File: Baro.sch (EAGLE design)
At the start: 9 parts

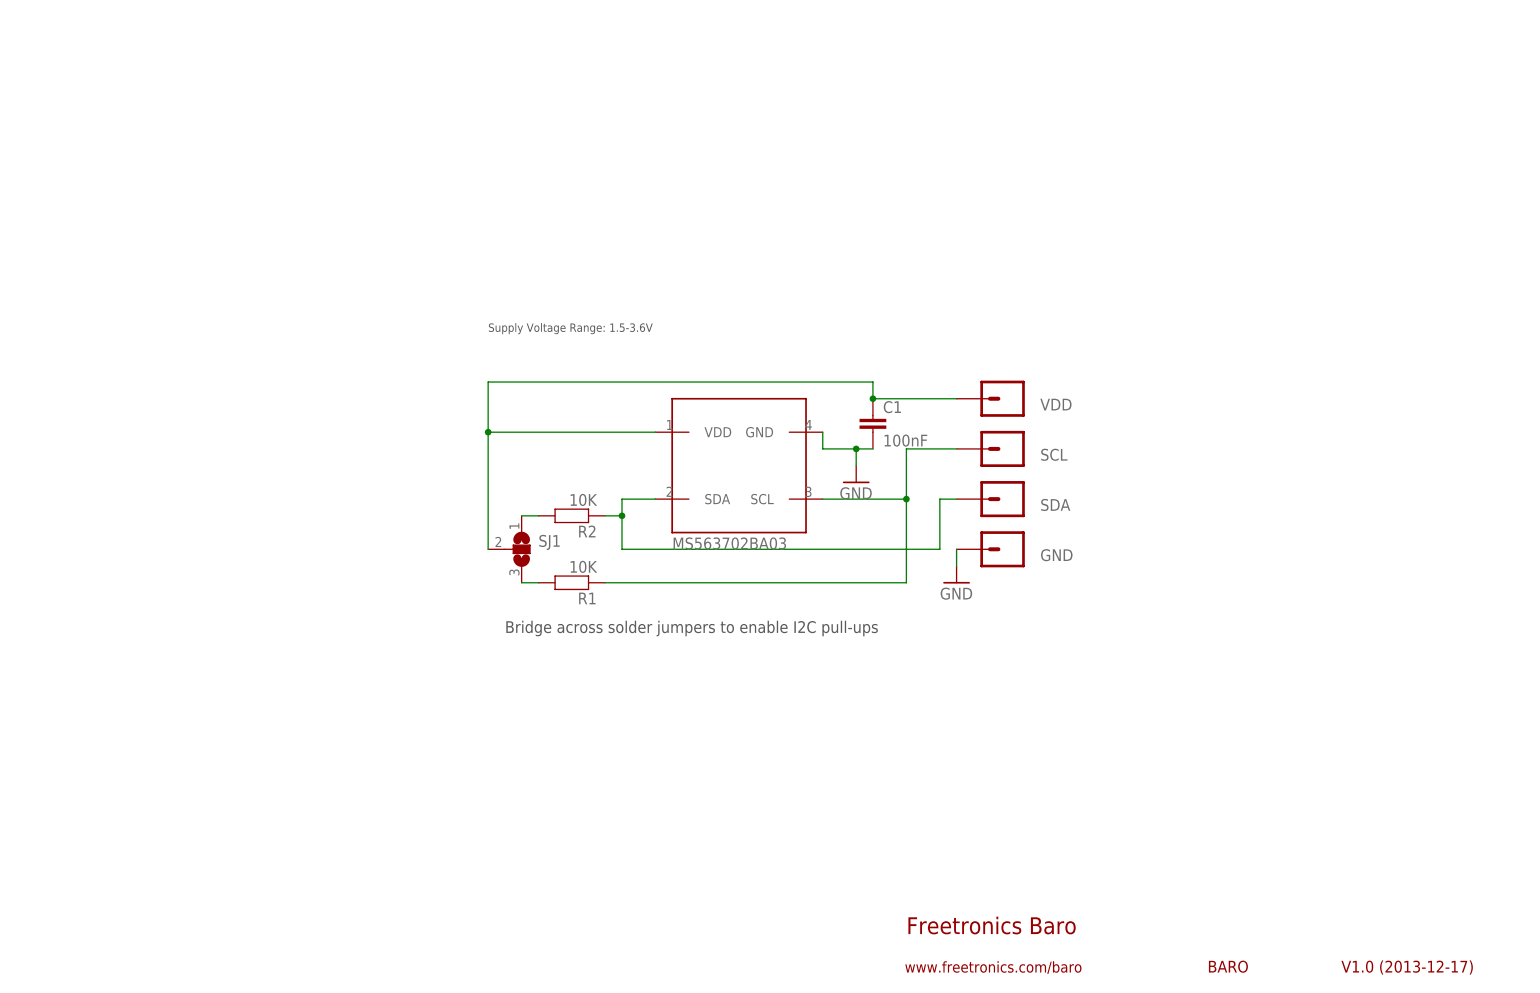
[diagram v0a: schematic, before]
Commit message: Volt. regulator and FETs added.
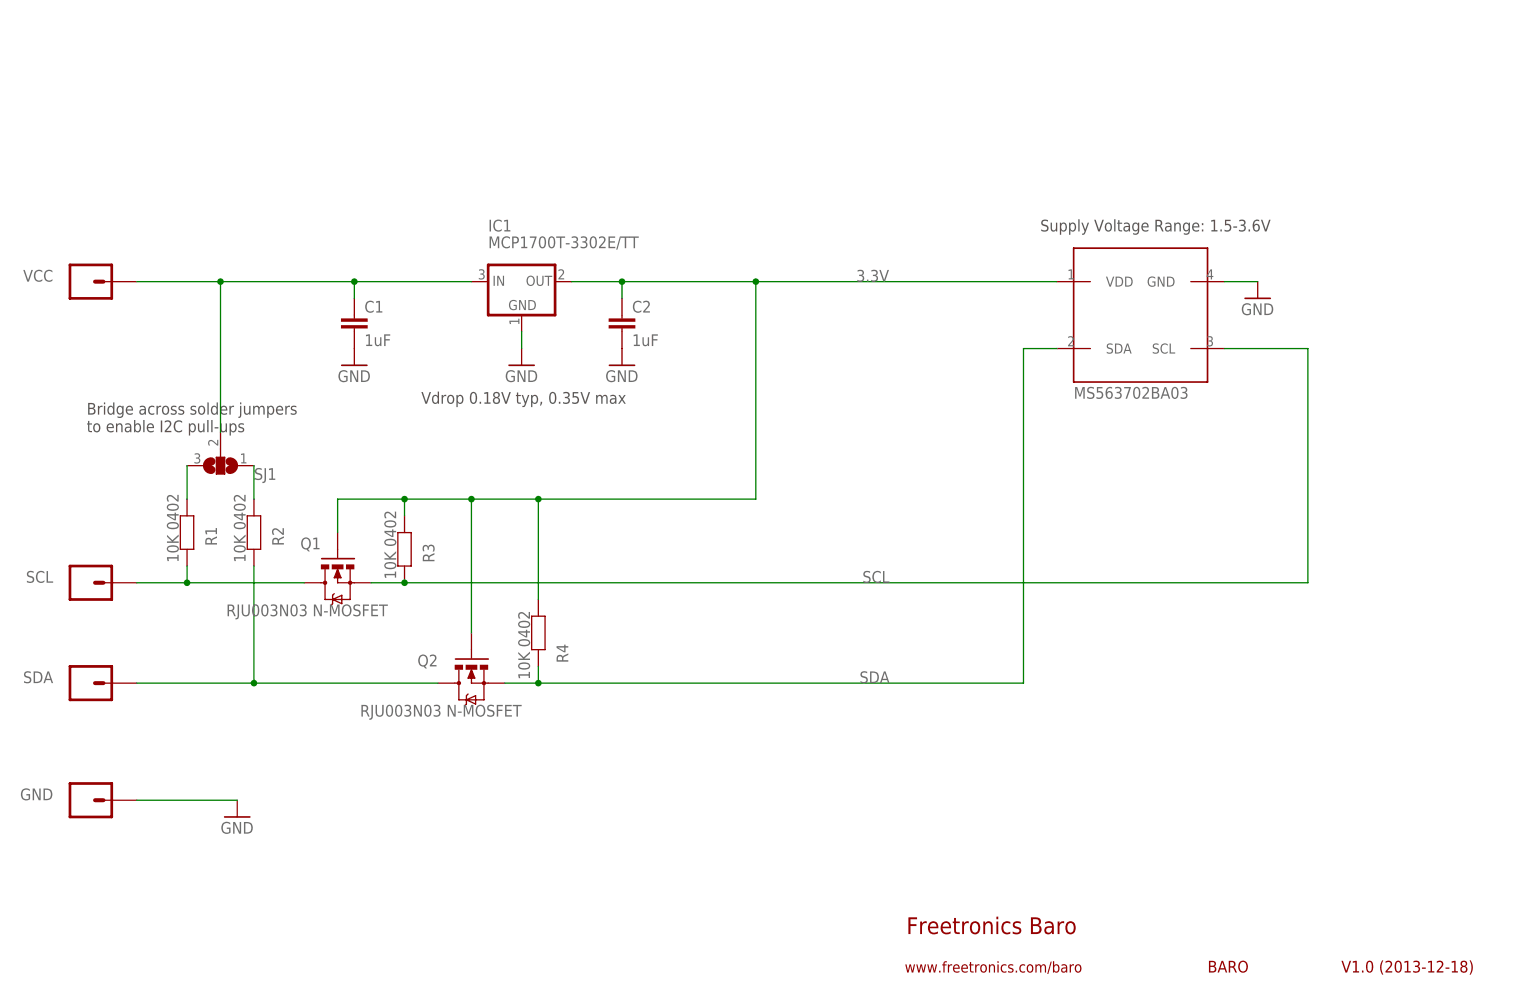
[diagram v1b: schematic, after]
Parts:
- removed VDD: M01PTH, freetronics-master-v1.1:M01PTH
- added C2: 1uF, freetronics-master-v1:CAP0603
- added IC1: MCP1700T-3302E/TT, freetronics-master-v1:V_REG_78XXSOT23-3
- added Q1, Q2: RJU003N03 N-MOSFET, freetronics-jon:MOSFET-NSOT-323
- added R3, R4: 10K 0402, freetronics-jon:RESISTOR0402
- added VCC: M01PTH, freetronics-master-v1.1:M01PTH
- C1: value 100nF -> 1uF; device freetronics-master-v1.1:CAP0603 -> freetronics-master-v1:CAP0603
- R1, R2: value 10K -> 10K 0402; device freetronics-master-v1.1:RESISTOR0603 -> freetronics-jon:RESISTOR0402
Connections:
- removed net N$2: C1.1, MS5637.VDD, SJ1.2, VDD.1
- new net 3.3V: C2.1, IC1.OUT, MS5637.VDD, Q1.G, Q2.G, R3.2, R4.2
- new net N$3: C1.1, IC1.IN, SJ1.2, VCC.1
- new net SCL: Q1.D, R1.1, SCL.1
- new net SDA: Q2.D, R2.1, SDA.1
- net GND: now also C2.2, IC1.GND
- net N$1: now also Q1.S, R3.1; no longer R1.1, SCL.1
- net N$4: now also Q2.S, R4.1; no longer R2.1, SDA.1
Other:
- note added: "V1.0 (2013-12-18)"
- note added: "Vdrop 0.18V typ, 0.35V max"
- note removed: "V1.0 (2013-12-17)"
- moved on the sheet: C1, GND, R1, R2, SCL, SDA, SJ1

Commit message: Noted Adelmo Eloy as the designer Added license info to schematic Relocated decoupling cap to near sensor Improved ground connection to regulator Added notes to schematic about operating ranges Changed I2C pull-ups to 4K7
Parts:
- removed GND, SCL, SDA, VCC: M01PTH, freetronics-master-v1.1:M01PTH
- removed MS5637: MS563702BA03, freetronics-original:MS563702BA03
- added H1: GND, freetronics-master-v1.1:M01PTH
- added H2: SDA, freetronics-master-v1.1:M01PTH
- added H3: SCL, freetronics-master-v1.1:M01PTH
- added H4: VCC, freetronics-master-v1.1:M01PTH
- added IC2: MS563702BA03, freetronics-original:MS563702BA03
- R1, R2: value 10K 0402 -> 4K7 0402
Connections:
- net 3.3V: now also IC2.VDD; no longer MS5637.VDD
- net GND: now also H1.1, IC2.GND; no longer GND.1, MS5637.GND
- net N$1: now also IC2.SCL; no longer MS5637.SCL
- net N$3: now also H4.1; no longer VCC.1
- net N$4: now also IC2.SDA; no longer MS5637.SDA
- net SCL: now also H3.1; no longer SCL.1
- net SDA: now also H2.1; no longer SDA.1
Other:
- note added: "Copyright 2014 Freetronics Pty Ltd Designed by Adelmo Eloy Released under the TAPR Open Hardware License www.tapr.org/OHL"
- note added: "Freetronics Barometric Pressure / Temp Sensor"
- note added: "Operating voltage: 2.3 - 6Vdc Pressure range: 1kpa to 200kpa (0.145psi to 29psi) Temperature range: -40C to +85C I2C address: 0xED Sensor: MS5637-02BA03"
- note added: "SKU: BARO"
- note added: "Sensor supply voltage: 1.5-3.6V"
- note removed: "BARO"
- note removed: "Freetronics Baro"
- note removed: "Supply Voltage Range: 1.5-3.6V"
- moved on the sheet: C1, C2, IC1, Q1, Q2, R1, R2, R3, R4, SJ1

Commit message: Fixed revision date
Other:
- note added: "V1.0 (2014-01-21)"
- note removed: "V1.0 (2013-12-18)"
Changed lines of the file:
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@@
 <plain>
 <text x="142.24" y="12.7" size="2.54" layer="94">Freetronics Barometric Pressure / Temp Sensor</text>
-<text x="215.9" y="6.858" size="1.778" layer="94">V1.0 (2013-12-18)</text>
+<text x="215.9" y="6.858" size="1.778" layer="94">V1.0 (2014-01-21)</text>
 <text x="141.986" y="6.858" size="1.651" layer="94">www.freetronics.com/baro</text>
 <text x="195.58" y="6.858" size="1.778" layer="94">SKU: BARO</text>
